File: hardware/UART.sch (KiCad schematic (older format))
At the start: 9 parts, among them J4 DB9_Female_MountingHoles, U14 MAX202

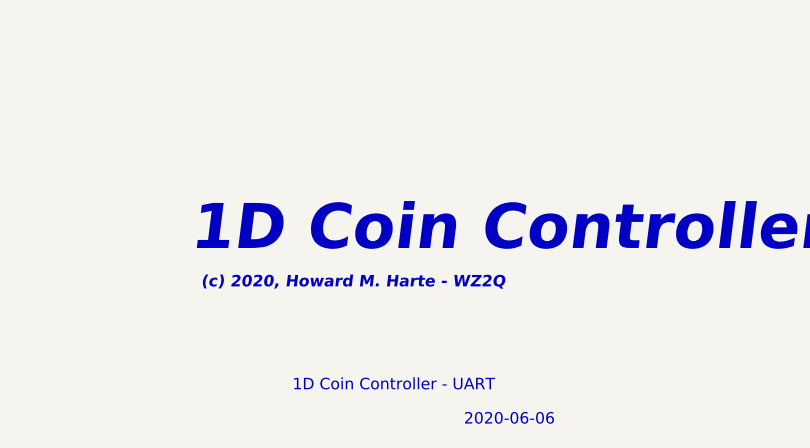
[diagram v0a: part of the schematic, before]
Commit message: Issue 2 schmatic and Layout
Added polarity reversal detection to monitor answer supervision.
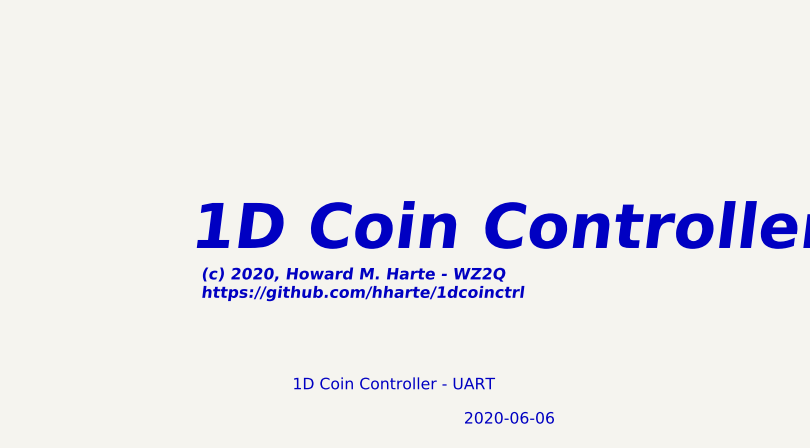
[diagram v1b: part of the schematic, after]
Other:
- note added: "(c) 2020, Howard M. Harte - WZ2Q\nhttps://github.com/hharte/1dcoinctrl"
- note removed: "(c) 2020, Howard M. Harte - WZ2Q"
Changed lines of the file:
@@
 Text Notes 7050 6900 0    197  Italic 39
 1D Coin Controller
-Text Notes 7100 7050 0    50   Italic 10
-(c) 2020, Howard M. Harte - WZ2Q
 Text Notes 10600 7650 0    50   ~ 0
 1
+Text Notes 7100 7100 0    50   Italic 10
+(c) 2020, Howard M. Harte - WZ2Q\nhttps://github.com/hharte/1dcoinctrl
 $EndSCHEMATC
